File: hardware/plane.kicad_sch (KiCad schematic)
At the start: 42 parts, among them J1 USB_B_Micro, J2 Conn_Coaxial, J3 Conn_01x03, J4 Conn_01x03, J5 Conn_01x03, J6 Conn_01x03, Q1 BSS138, Q2 BSS138, U1 ESP32-WROOM-32, U2 AMS1117-3.3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

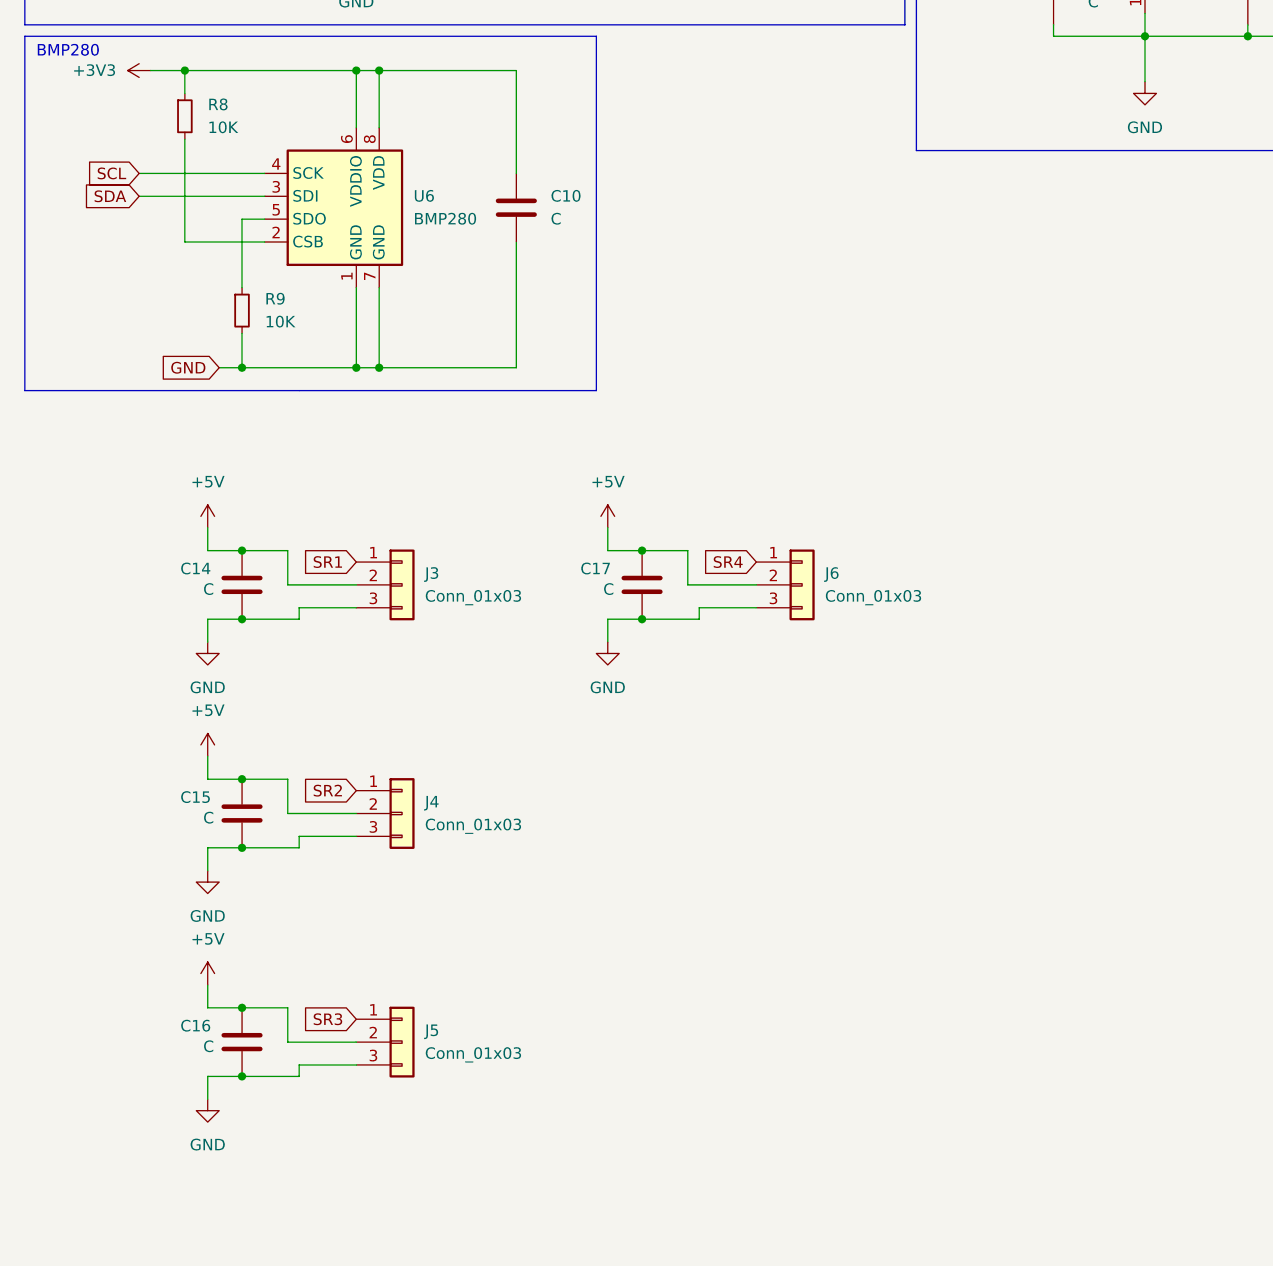
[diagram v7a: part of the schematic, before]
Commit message: wiring + battery connector
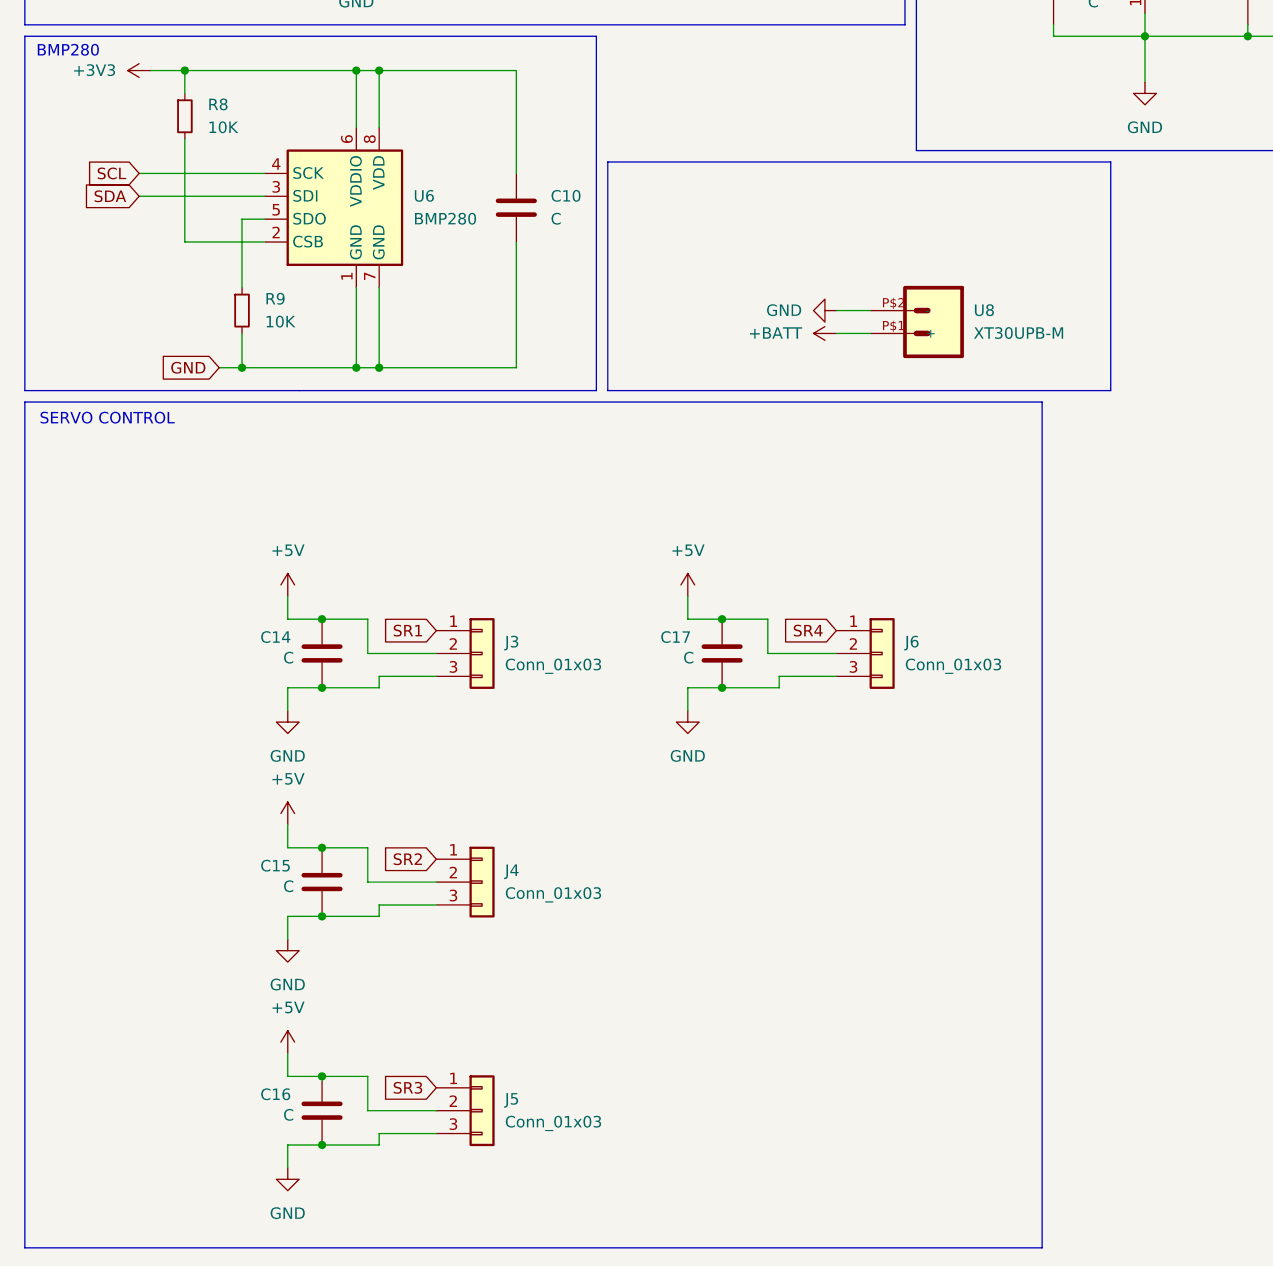
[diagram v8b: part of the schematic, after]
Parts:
- added U8: XT30UPB-M, XT30UPB-M:XT30UPB-M, symbol XT30:XT30UPB-M
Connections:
- net +BATT: now also U8.P$1 (+)
- net GND: now also U8.P$2 (-)
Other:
- note added: "SERVO CONTROL"
- moved on the sheet: C14, C15, C16, C17, J3, J4, J5, J6
